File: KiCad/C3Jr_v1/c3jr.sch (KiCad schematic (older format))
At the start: 33 parts, among them P43 CONN_1, Q17 2N5401, SW1 INC, SW2 DEC, SW3 MODE, SW4 RST, SW5 ENTER, U3 ATMEGA8-P, U4 74LS154, U5 STP8DP05, X1 16MHz

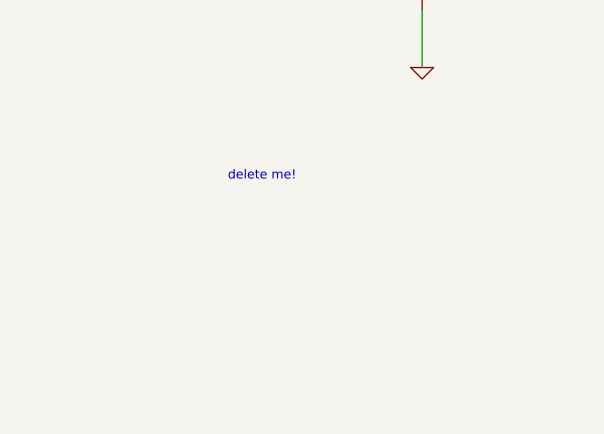
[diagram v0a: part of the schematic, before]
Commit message: C3Jr_v1 : Clean up of OLD C3jr_v1 files. Added PCB module to get better 3D views
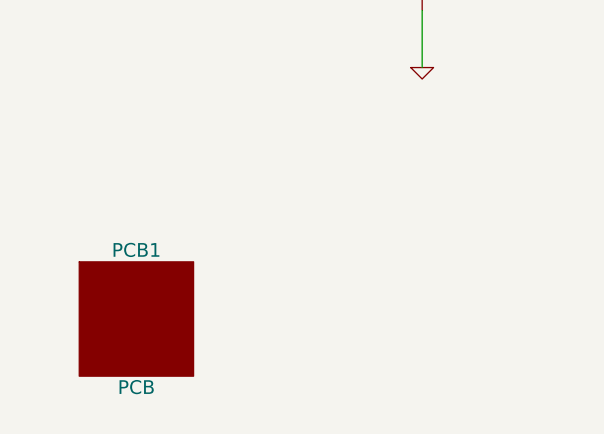
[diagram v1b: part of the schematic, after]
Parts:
- added PCB1: PCB, symbol PCB
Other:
- note removed: "delete me!"
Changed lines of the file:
@@
-EESchema Schematic File Version 2  date 11/23/2011 4:10:03 PM
+EESchema Schematic File Version 2  date 3/19/2012 5:46:04 PM
 LIBS:C3Jr_v1
 LIBS:power
+LIBS:c3jr-cache
 LIBS:c3jr-cache
 EELAYER 25  0
@@
 Sheet 1 4
 Title "ClockTHREE Junior aka C3Jr"
-Date "21 nov 2011"
+Date "19 mar 2012"
 Rev "A"
 Comp "an improved WordClock based on ClockTHREE"
@@
 Comment4 ""
 $EndDescr
-Text Notes 1500 6600 0    40   ~ 0
-delete me!
+$Comp
+L PCB PCB1
+U 1 1 4F672369
+P 1100 7200
+F 0 "PCB1" H 1100 7500 60  0000 C CNN
+F 1 "PCB" H 1100 6900 60  0000 C CNN
+	1    1100 7200
+	1    0    0    -1
+$EndComp
 Wire Wire Line
 	700  4700 700  4800
